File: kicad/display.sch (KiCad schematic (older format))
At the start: 33 parts

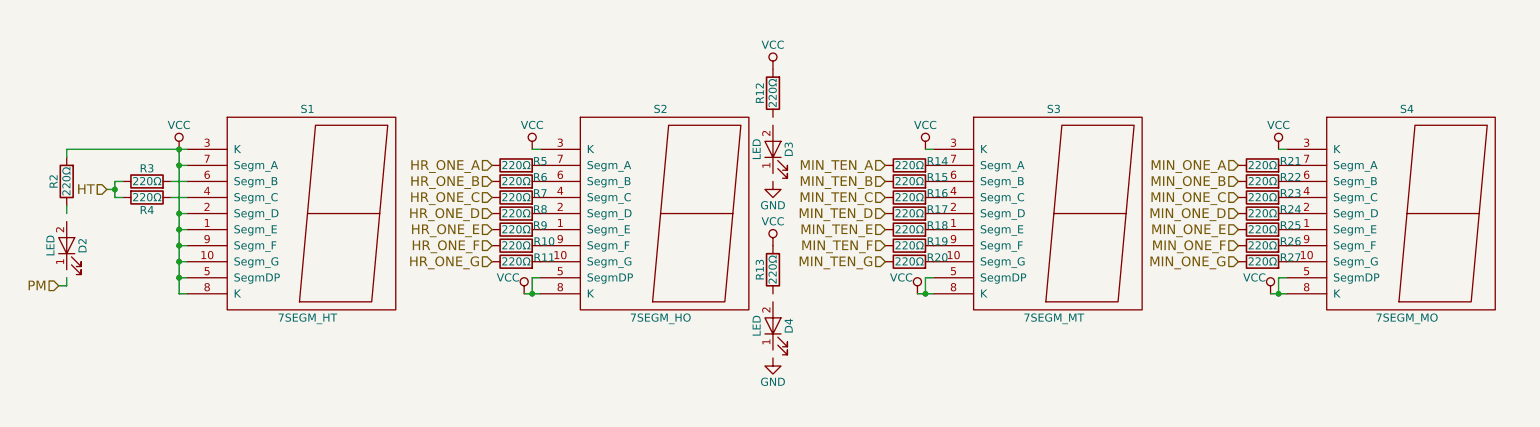
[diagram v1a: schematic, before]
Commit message: Add BoM, update component info, use 150Ohm current limiting resistors, update layout respectively
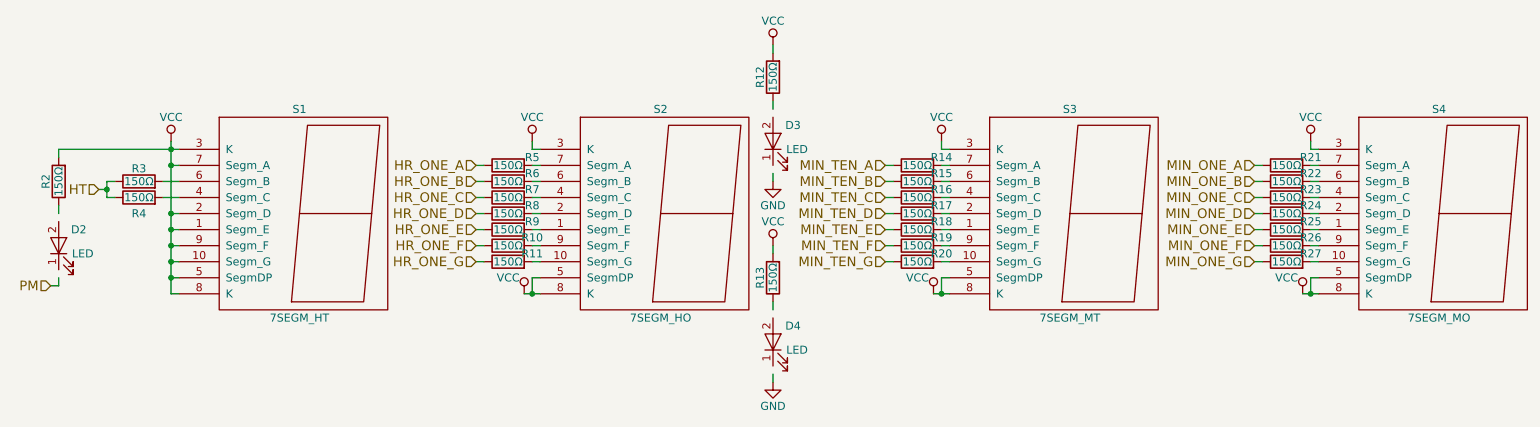
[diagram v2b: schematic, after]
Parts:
- D2, D3, D4: Distrib Link (none) -> http://www.digikey.com/product-detail/en/lite-on-inc/LTST-C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; Distrib PN (none) -> 160-1427-1-ND; MFG Name (none) -> Lite-On; MFG Part Num (none) -> LTST-C171KRKT; Others (none) -> http://www.digikey.com/products/en/optoelectronics/led-indi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; Tolerance (none) -> -
- R10, R11, R12, R13, R14, R15, R16, R17, R18, R19, R2, R20, R21, R22, R23, R24, R25, R26, R27, R3, R4, R5, R6, R7, R8, R9: value 220Ω -> 150Ω; Distrib Link (none) -> http://www.digikey.com/product-detail/en/stackpole-electron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; Distrib PN (none) -> RMCF0805JT150RCT-ND; MFG Name (none) -> Stackpole Electronics; MFG Part Num (none) -> RMCF0805JT150R; Others (none) -> http://www.digikey.com/products/en/resistors/chip-resistor-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; Tolerance (none) -> 5%
- S1, S2, S3, S4: Others (none) -> -; Tolerance (none) -> -
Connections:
- wire segments 31 -> 82
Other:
- moved on the sheet: S1, S3, S4
